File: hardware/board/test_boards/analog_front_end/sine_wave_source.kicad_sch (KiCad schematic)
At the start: 15 parts, among them U7 AD9833xRM, U8 LTC6263, X1 ECS-TXO-2016

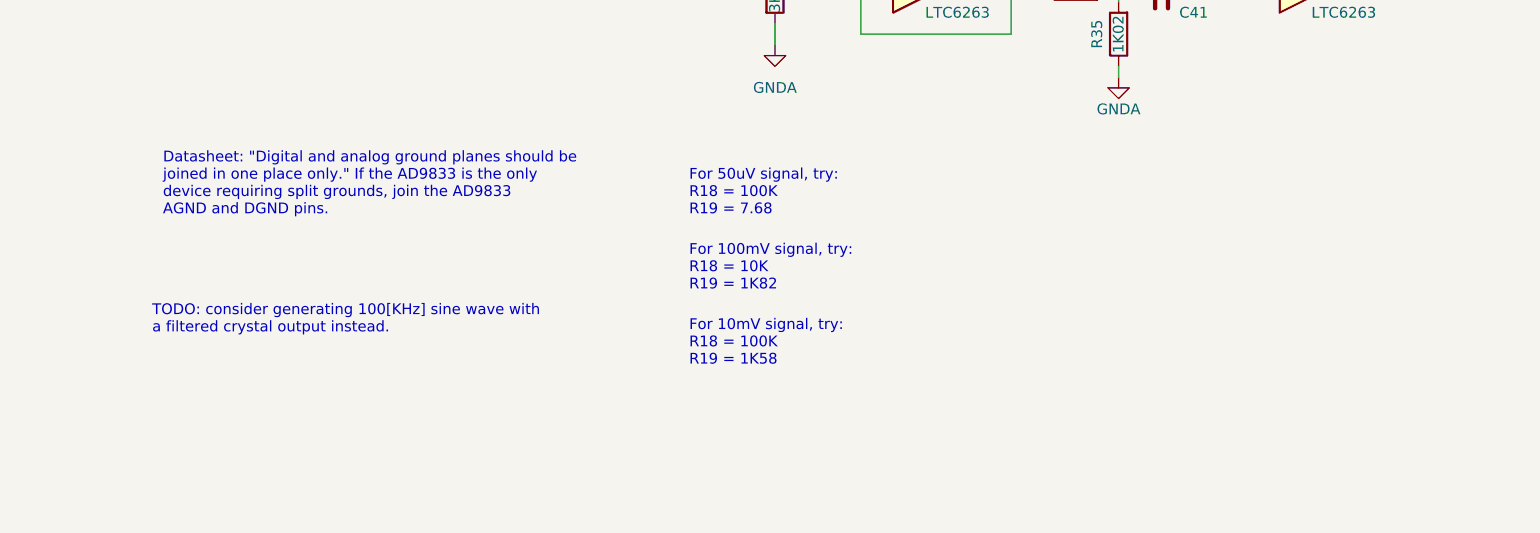
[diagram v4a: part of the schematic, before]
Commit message: draft ads7029 pio driver
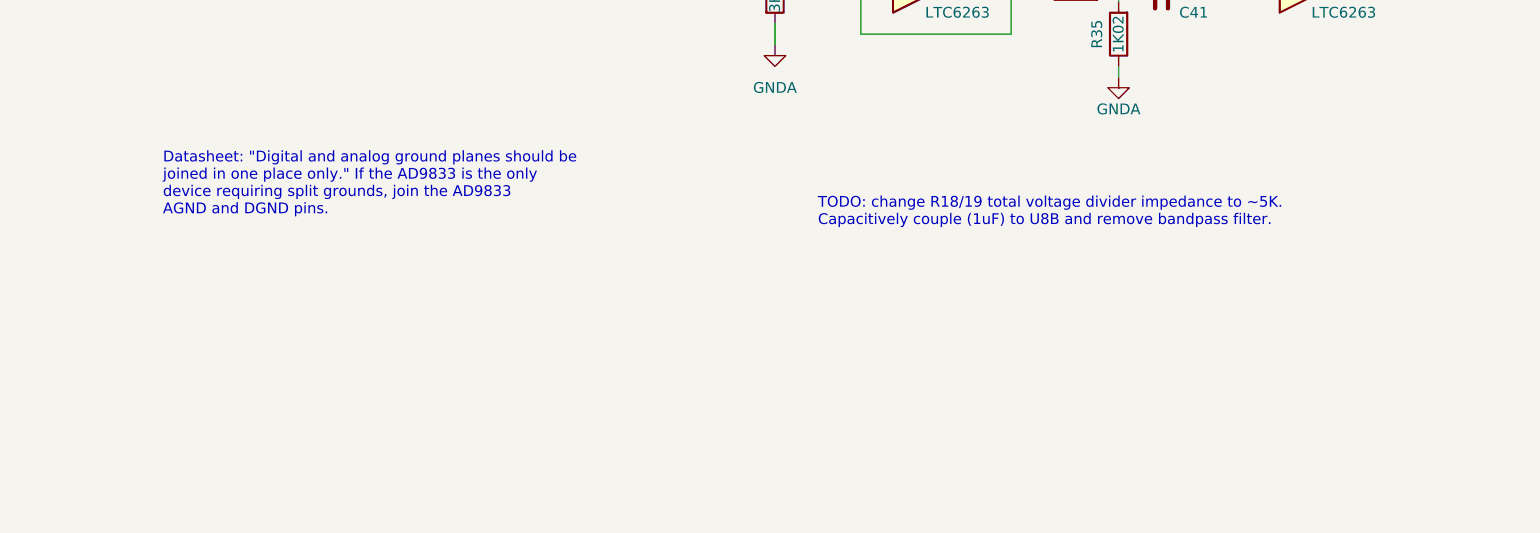
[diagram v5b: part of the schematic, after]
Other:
- note added: "TODO: change R18/19 total voltage divider impedance to ~5K. Capacitively couple (1uF) to U8B and remove bandpass filter."
- note removed: "For 100mV signal, try: R18 = 10K R19 = 1K82"
- note removed: "For 10mV signal, try: R18 = 100K R19 = 1K58"
- note removed: "For 50uV signal, try: R18 = 100K R19 = 7.68"
- note removed: "TODO: consider generating 100[KHz] sine wave with a filtered crystal output instead."
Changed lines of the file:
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@@
     (effects (font (size 1.27 1.27)) (justify left bottom))
   )
-  (text "For 10mV signal, try: \nR18 = 100K\nR19 = 1K58" (at 162.56 157.48 0)
-    (effects (font (size 1.27 1.27)) (justify left bottom))
-  )
-  (text "TODO: consider generating 100[KHz] sine wave with \na filtered crystal output instead."
-    (at 99.06 153.67 0)
+  (text "TODO: change R18/19 total voltage divider impedance to ~5K.\nCapacitively couple (1uF) to U8B and remove bandpass filter."
+    (at 177.8 140.97 0)
     (effects (font (size 1.27 1.27)) (justify left bottom))
   )
@@
     (effects (font (size 1.27 1.27)) (justify left bottom))
   )
-  (text "For 50uV signal, try: \nR18 = 100K\nR19 = 7.68" (at 162.56 139.7 0)
-    (effects (font (size 1.27 1.27)) (justify left bottom))
-  )
   (text "Oscillator \nBypass Cap" (at 20.32 158.75 0)
     (effects (font (size 1.27 1.27)) (justify left bottom))
@@
     (effects (font (size 1.27 1.27)) (justify left bottom))
   )
-  (text "For 100mV signal, try: \nR18 = 10K\nR19 = 1K82" (at 162.56 148.59 0)
-    (effects (font (size 1.27 1.27)) (justify left bottom))
-  )
